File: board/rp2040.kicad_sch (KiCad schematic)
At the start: 22 parts, among them U1 W25Q128JVS, U2 RP2040, Y1 12MhZ

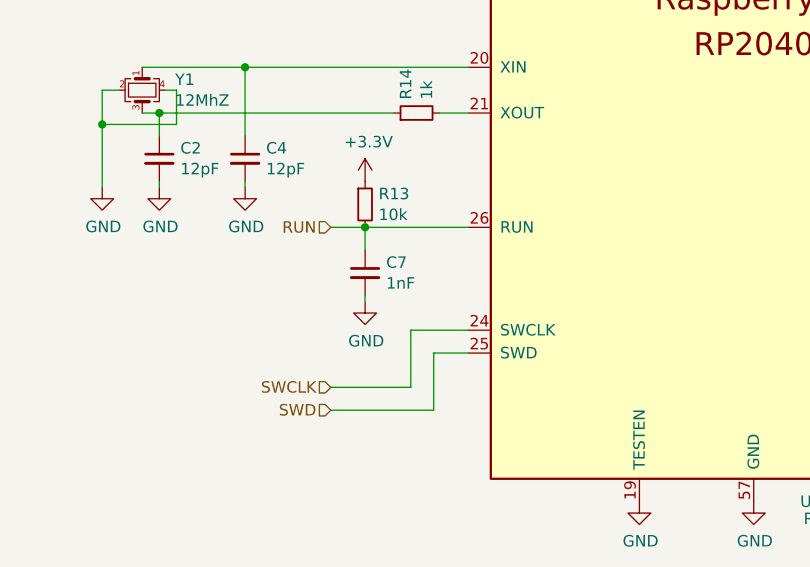
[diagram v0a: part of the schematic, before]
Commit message: added needle addapter
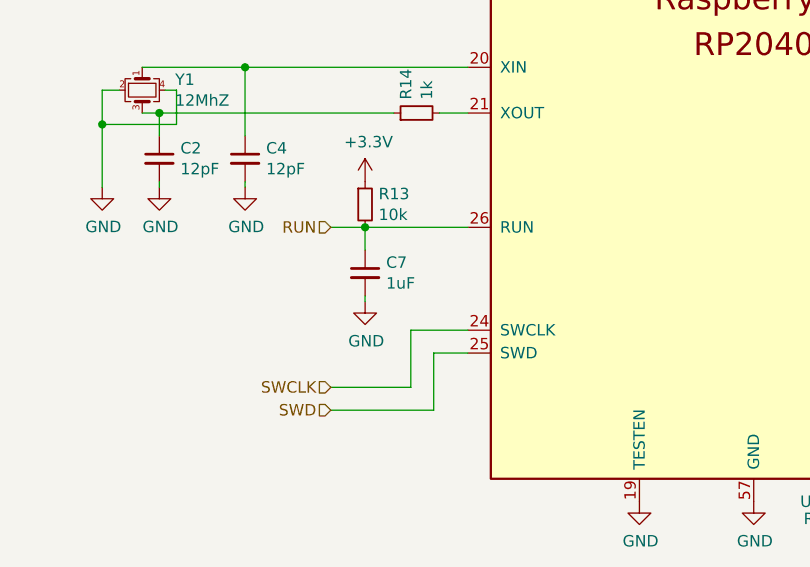
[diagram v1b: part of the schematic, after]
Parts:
- C7: value 1nF -> 1uF
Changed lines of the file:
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@@
       (effects (font (size 1.27 1.27)) (justify left))
     )
-    (property "Value" "1nF" (id 1) (at 92.5068 135.763 0)
+    (property "Value" "1uF" (id 1) (at 92.5068 135.763 0)
       (effects (font (size 1.27 1.27)) (justify left))
     )

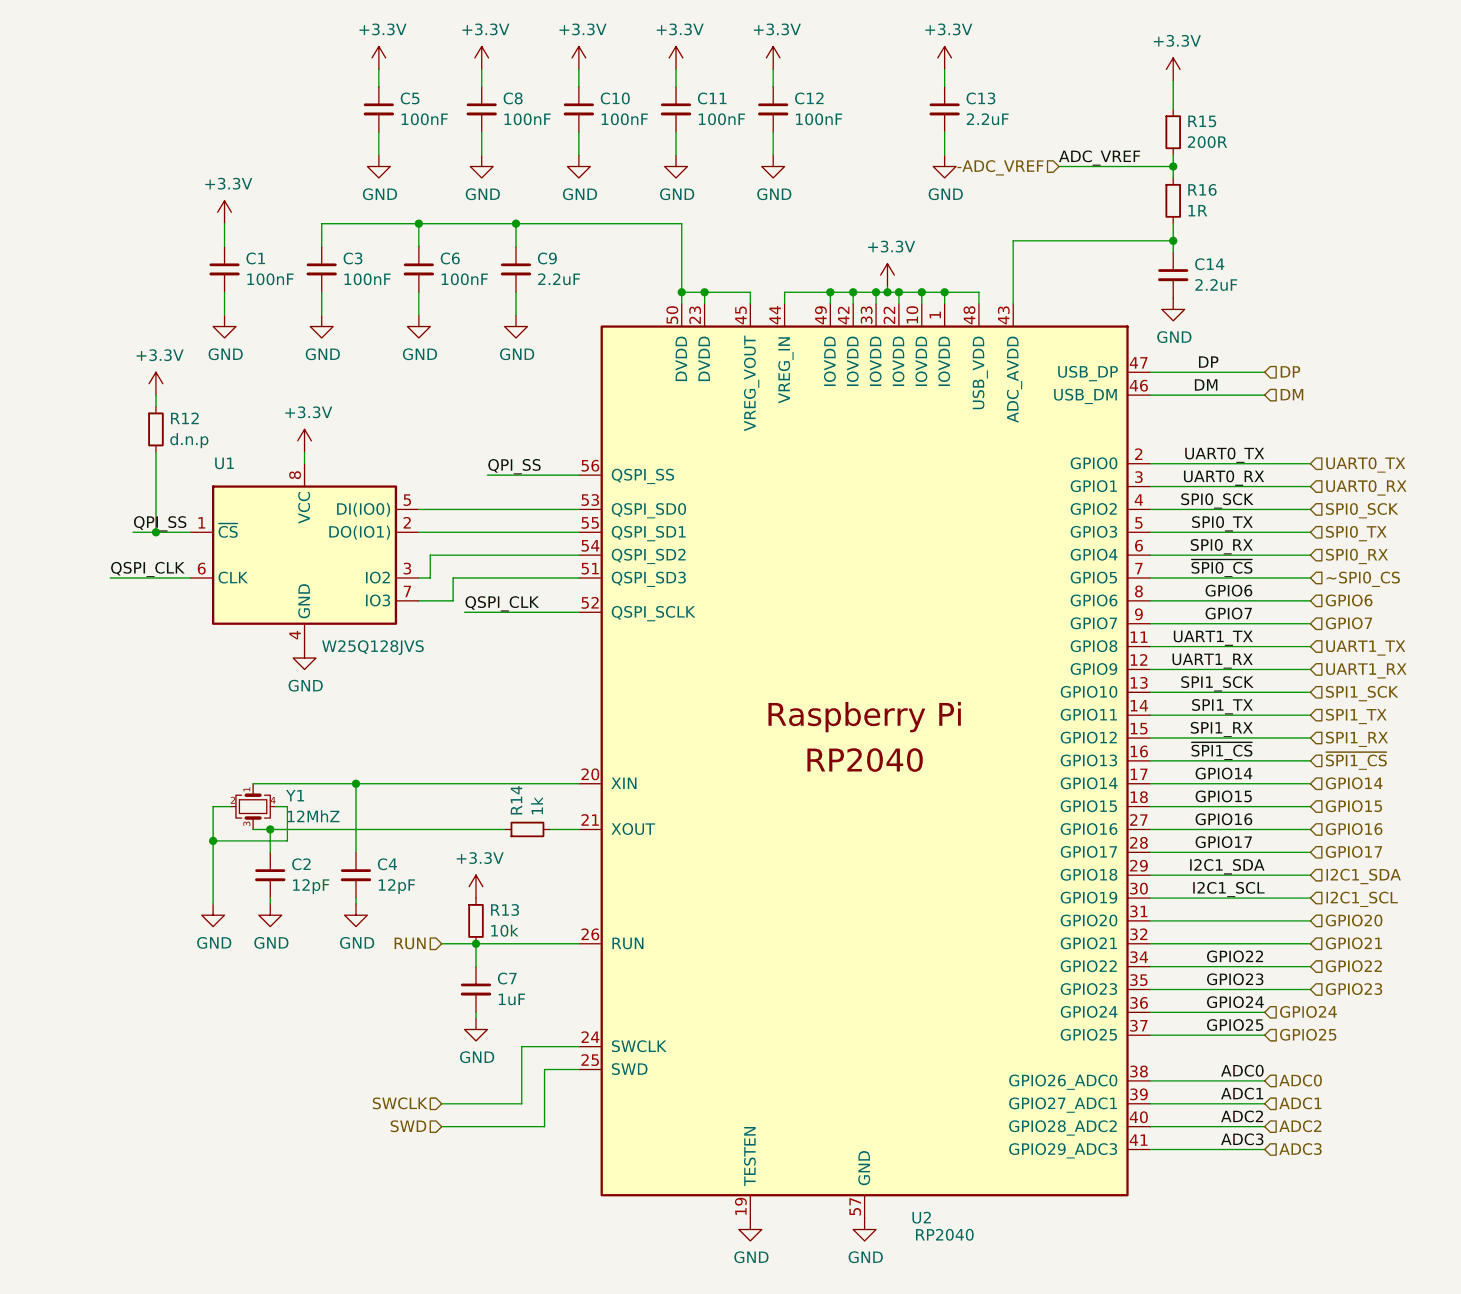
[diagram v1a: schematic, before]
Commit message: improved power integrity
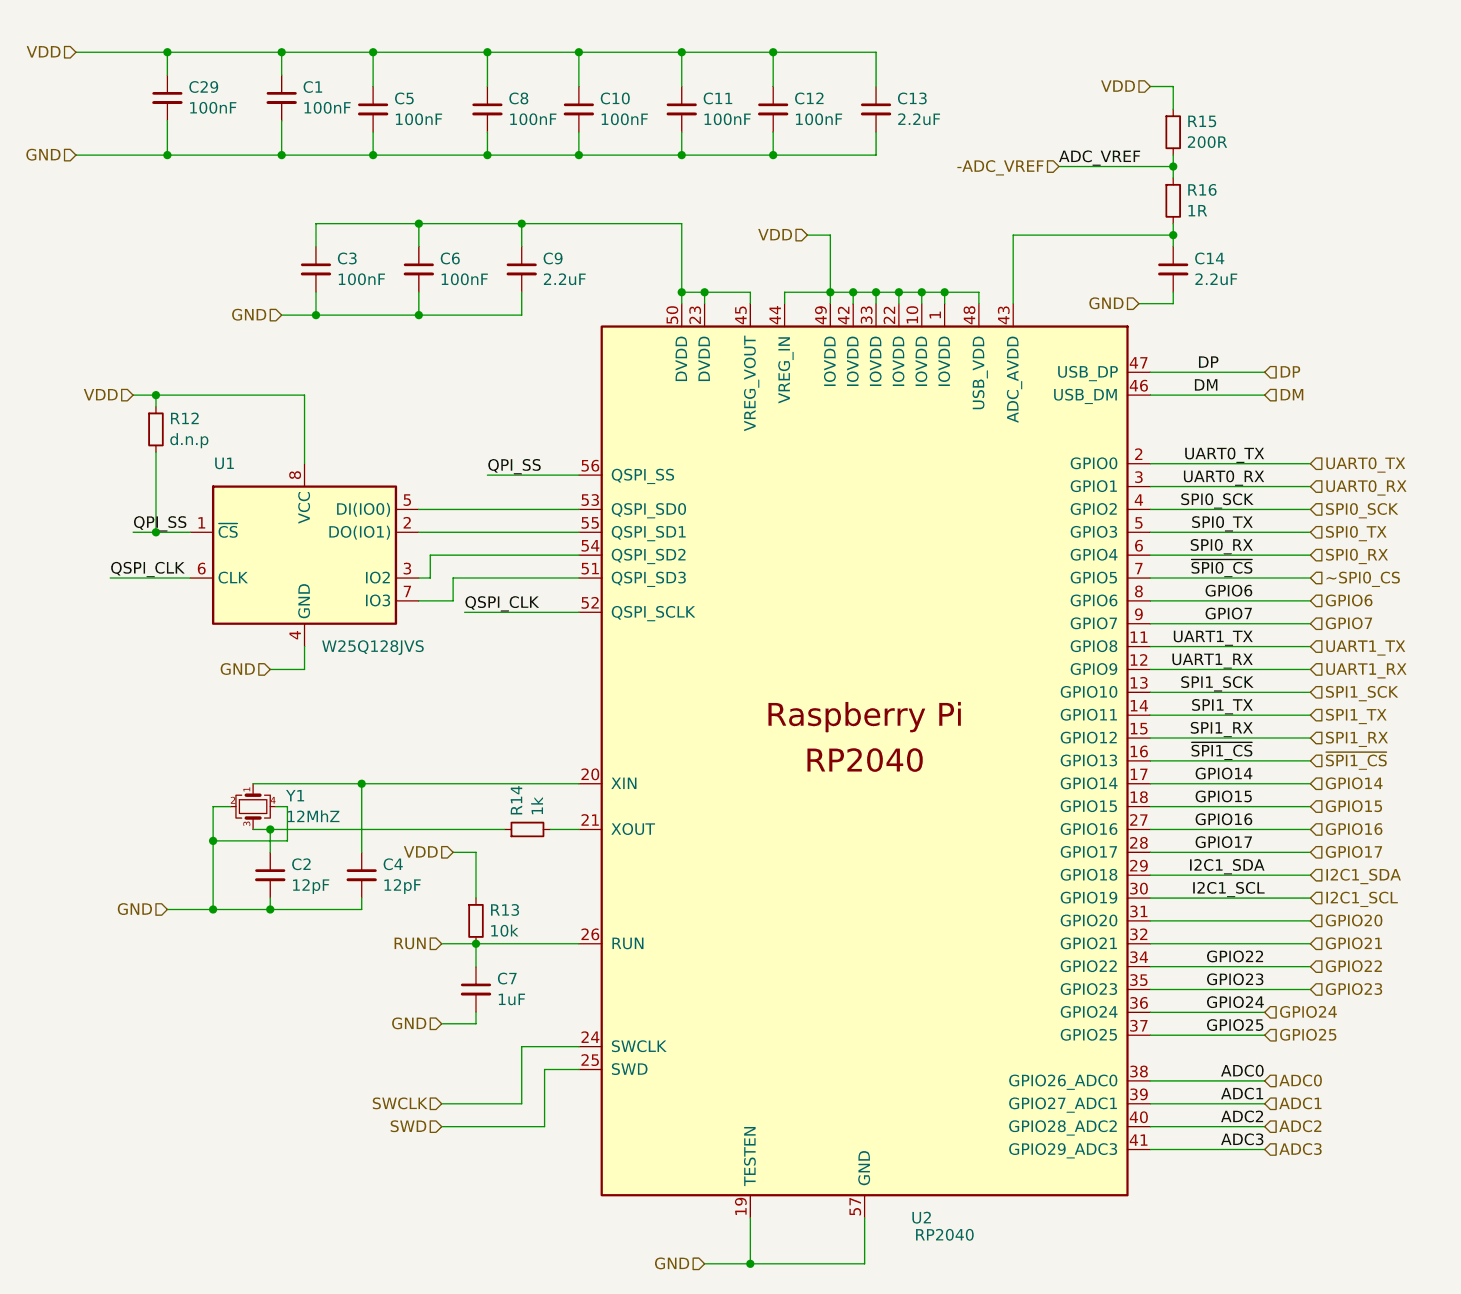
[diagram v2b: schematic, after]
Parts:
- added C29: 100nF, Capacitor_SMD:C_0603_1608Metric, symbol Device:C_Small
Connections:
- net GND: now also C29.2
- net +3V3 renamed VDD
- net VDD: now also C29.1
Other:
- moved on the sheet: C1, C11, C13, C14, C3, C4, C5, C8, C9

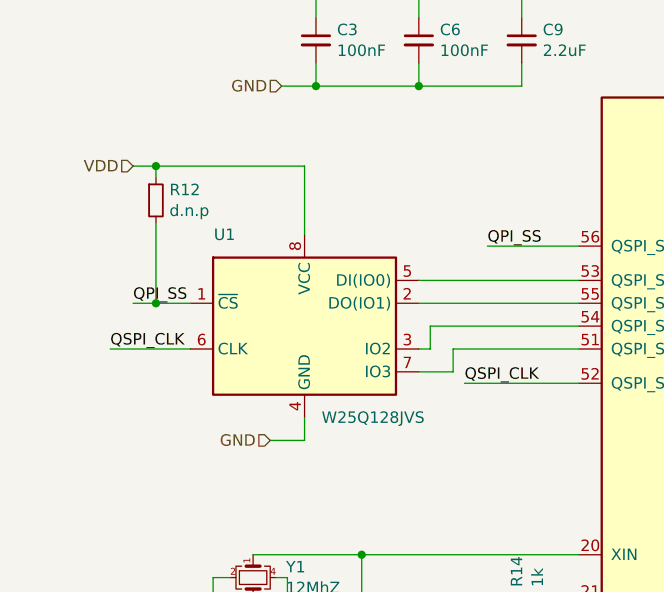
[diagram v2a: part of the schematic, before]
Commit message: added boot select button and standard (small) flash
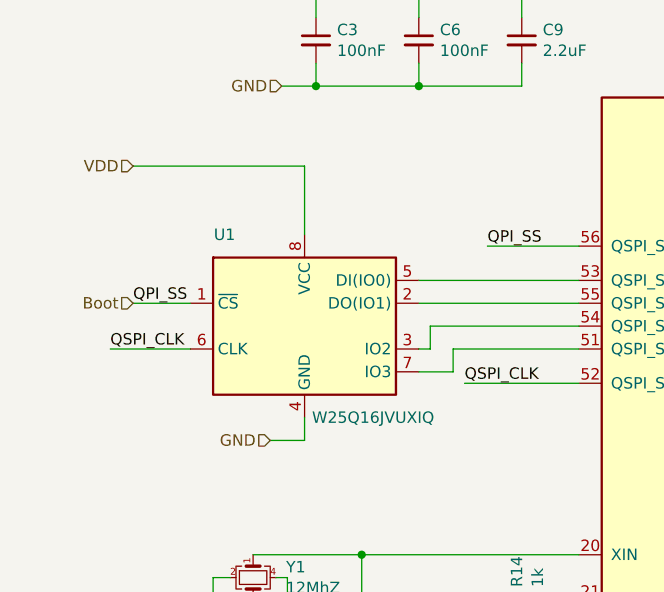
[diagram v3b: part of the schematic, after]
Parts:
- removed R12: d.n.p, Resistor_SMD:R_0603_1608Metric, symbol Device:R_Small
- U1: value W25Q128JVS -> W25Q16JVUXIQ; footprint Package_SO:SOIC-8_5.23x5.23mm_P1.27mm -> Package_DFN_QFN:DFN-8-1EP_3x2mm_P0.5mm_EP1.3x1.5mm
- U2: footprint b018:RP2040-QFN-56 -> Package_DFN_QFN:QFN-56-1EP_7x7mm_P0.4mm_EP3.2x3.2mm
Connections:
- net QPI_SS renamed Boot

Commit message: moved all components to top layer
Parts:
- C1, C10, C11, C12, C13, C14, C29, C3, C5, C6, C7, C8, C9: footprint Capacitor_SMD:C_0603_1608Metric -> Capacitor_SMD:C_0402_1005Metric
- R13, R14: footprint Resistor_SMD:R_0603_1608Metric -> Resistor_SMD:R_0402_1005Metric
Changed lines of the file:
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@@
       (effects (font (size 1.27 1.27)) (justify left))
     )
-    (property "Footprint" "Capacitor_SMD:C_0603_1608Metric" (at 55.88 35.56 0)
+    (property "Footprint" "Capacitor_SMD:C_0402_1005Metric" (at 55.88 35.56 0)
       (effects (font (size 1.27 1.27)) hide)
     )
@@
       (effects (font (size 1.27 1.27)) (justify left))
     )
-    (property "Footprint" "Capacitor_SMD:C_0603_1608Metric" (at 113.03 36.83 0)
+    (property "Footprint" "Capacitor_SMD:C_0402_1005Metric" (at 113.03 36.83 0)
       (effects (font (size 1.27 1.27)) hide)
     )
@@
       (effects (font (size 1.27 1.27)) (justify left))
     )
-    (property "Footprint" "Capacitor_SMD:C_0603_1608Metric" (at 134.62 36.83 0)
+    (property "Footprint" "Capacitor_SMD:C_0402_1005Metric" (at 134.62 36.83 0)
       (effects (font (size 1.27 1.27)) hide)
     )
@@
       (effects (font (size 1.27 1.27)) (justify left))
     )
-    (property "Footprint" "Capacitor_SMD:C_0603_1608Metric" (at 95.25 54.61 0)
+    (property "Footprint" "Capacitor_SMD:C_0402_1005Metric" (at 95.25 54.61 0)
       (effects (font (size 1.27 1.27)) hide)
     )
@@
       (effects (font (size 1.27 1.27)) (justify left))
     )
-    (property "Footprint" "Capacitor_SMD:C_0603_1608Metric" (at 101.6 36.83 0)
+    (property "Footprint" "Capacitor_SMD:C_0402_1005Metric" (at 101.6 36.83 0)
       (effects (font (size 1.27 1.27)) hide)
     )
@@
       (effects (font (size 1.27 1.27)) (justify left))
     )
-    (property "Footprint" "Capacitor_SMD:C_0603_1608Metric" (at 78.74 36.83 0)
+    (property "Footprint" "Capacitor_SMD:C_0402_1005Metric" (at 78.74 36.83 0)
       (effects (font (size 1.27 1.27)) hide)
     )
@@
       (effects (font (size 1.27 1.27)) (justify left))
     )
-    (property "Footprint" "Capacitor_SMD:C_0603_1608Metric" (at 90.17 134.62 0)
+    (property "Footprint" "Capacitor_SMD:C_0402_1005Metric" (at 90.17 134.62 0)
       (effects (font (size 1.27 1.27)) hide)
     )
@@
       (effects (font (size 1.27 1.27)) (justify left))
     )
-    (property "Footprint" "Capacitor_SMD:C_0603_1608Metric" (at 123.19 36.83 0)
+    (property "Footprint" "Capacitor_SMD:C_0402_1005Metric" (at 123.19 36.83 0)
       (effects (font (size 1.27 1.27)) hide)
     )
@@
       (effects (font (size 1.27 1.27)) (justify left))
     )
-    (property "Footprint" "Resistor_SMD:R_0603_1608Metric" (at 90.17 127 0)
+    (property "Footprint" "Resistor_SMD:R_0402_1005Metric" (at 90.17 127 0)
       (effects (font (size 1.27 1.27)) hide)
     )
@@
       (effects (font (size 1.27 1.27)) (justify left))
     )
-    (property "Footprint" "Capacitor_SMD:C_0603_1608Metric" (at 167.64 54.61 0)
+    (property "Footprint" "Capacitor_SMD:C_0402_1005Metric" (at 167.64 54.61 0)
       (effects (font (size 1.27 1.27)) hide)
     )
@@
       (effects (font (size 1.27 1.27)) (justify left))
     )
-    (property "Footprint" "Capacitor_SMD:C_0603_1608Metric" (at 68.58 35.56 0)
+    (property "Footprint" "Capacitor_SMD:C_0402_1005Metric" (at 68.58 35.56 0)
       (effects (font (size 1.27 1.27)) hide)
     )
@@
       (effects (font (size 1.27 1.27)) (justify left))
     )
-    (property "Footprint" "Capacitor_SMD:C_0603_1608Metric" (at 91.44 36.83 0)
+    (property "Footprint" "Capacitor_SMD:C_0402_1005Metric" (at 91.44 36.83 0)
       (effects (font (size 1.27 1.27)) hide)
     )
@@
       (effects (font (size 1.27 1.27)) (justify left))
     )
-    (property "Footprint" "Capacitor_SMD:C_0603_1608Metric" (at 83.82 54.61 0)
+    (property "Footprint" "Capacitor_SMD:C_0402_1005Metric" (at 83.82 54.61 0)
       (effects (font (size 1.27 1.27)) hide)
     )
@@
       (effects (font (size 1.27 1.27)) (justify left))
     )
-    (property "Footprint" "Resistor_SMD:R_0603_1608Metric" (at 95.885 116.84 0)
+    (property "Footprint" "Resistor_SMD:R_0402_1005Metric" (at 95.885 116.84 0)
       (effects (font (size 1.27 1.27)) hide)
     )
@@
       (effects (font (size 1.27 1.27)) (justify left))
     )
-    (property "Footprint" "Capacitor_SMD:C_0603_1608Metric" (at 72.39 54.61 0)
-      (effects (font (size 1.27 1.27)) hide)
-    )
+    (property "Footprint" "Capacitor_SMD:C_0402_1005Metric" (at 72.39 54.61 0)
+      (effects (font (size 1.27 1.27)) hide)
+    )

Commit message: added lcsc part numbers
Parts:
- C1, C10, C11, C12, C29, C3, C5, C6, C8: lcsc (none) -> C1525
- C13, C14, C9: lcsc (none) -> C12530
- C2, C4: lcsc (none) -> C1644
- C7: lcsc (none) -> C52923
- R13: lcsc (none) -> C25744
- R14: lcsc (none) -> C11702
- R15: lcsc (none) -> C8218
- R16: lcsc (none) -> C22936
- U1: lcsc (none) -> C2843335
- U2: lcsc (none) -> C2040
- Y1: lcsc (none) -> C9002
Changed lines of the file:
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@@
+      (effects (font (size 1.27 1.27)) hide)
+    )
+    (property "lcsc" "C1525" (at 55.88 35.56 0)
       (effects (font (size 1.27 1.27)) hide)
     )
@@
       (effects (font (size 1.27 1.27)) hide)
     )
+    (property "lcsc" "C1525" (at 113.03 36.83 0)
+      (effects (font (size 1.27 1.27)) hide)
+    )
     (pin "1")
     (pin "2")
@@
       (effects (font (size 1.27 1.27)) hide)
     )
+    (property "lcsc" "C12530" (at 134.62 36.83 0)
+      (effects (font (size 1.27 1.27)) hide)
+    )
     (pin "1")
     (pin "2")
@@
       (effects (font (size 1.27 1.27)) hide)
     )
+    (property "lcsc" "C8218" (at 167.64 39.37 0)
+      (effects (font (size 1.27 1.27)) hide)
+    )
     (pin "1")
     (pin "2")
@@
       (effects (font (size 1.27 1.27)) hide)
     )
+    (property "lcsc" "C12530" (at 95.25 54.61 0)
+      (effects (font (size 1.27 1.27)) hide)
+    )
     (pin "1")
     (pin "2")
@@
     )
     (property "Datasheet" "~" (at 101.6 36.83 0)
+      (effects (font (size 1.27 1.27)) hide)
+    )
+    (property "lcsc" "C1525" (at 101.6 36.83 0)
       (effects (font (size 1.27 1.27)) hide)
     )
@@
     )
     (property "Datasheet" "" (at 114.3 109.22 0)
+      (effects (font (size 1.27 1.27)) hide)
+    )
+    (property "lcsc" "C2040" (at 133.35 109.22 0)
       (effects (font (size 1.27 1.27)) hide)
     )
@@
       (effects (font (size 1.27 1.27)) hide)
     )
+    (property "lcsc" "C1525" (at 78.74 36.83 0)
+      (effects (font (size 1.27 1.27)) hide)
+    )
     (pin "1")
     (pin "2")
@@
       (effects (font (size 1.27 1.27)) hide)
     )
+    (property "lcsc" "C52923" (at 90.17 134.62 0)
+      (effects (font (size 1.27 1.27)) hide)
+    )
     (pin "1")
     (pin "2")
@@
     )
     (property "Datasheet" "~" (at 77.47 121.92 0)
+      (effects (font (size 1.27 1.27)) hide)
+    )
+    (property "lcsc" "C1644" (at 77.47 121.92 0)
       (effects (font (size 1.27 1.27)) hide)
     )
@@
     )
     (property "Datasheet" "https://www.winbond.com/resource-files/w25q16jv%20spi%20revh%2004082019%20plus.pdf" (at 71.12 86.36 0)
+      (effects (font (size 1.27 1.27)) hide)
+    )
+    (property "lcsc" "C2843335" (at 71.12 86.36 0)
       (effects (font (size 1.27 1.27)) hide)
     )
@@
       (effects (font (size 1.27 1.27)) hide)
     )
+    (property "lcsc" "C1525" (at 123.19 36.83 0)
+      (effects (font (size 1.27 1.27)) hide)
+    )
     (pin "1")
     (pin "2")
@@
     )
     (property "MPN" "ABM8G-12.000MHZ-4Y-T3" (at 65.405 114.3 90)
+      (effects (font (size 1.27 1.27)) hide)
+    )
+    (property "lcsc" "C9002" (at 65.405 114.3 0)
       (effects (font (size 1.27 1.27)) hide)
     )
@@
       (effects (font (size 1.27 1.27)) hide)
     )
+    (property "lcsc" "C25744" (at 90.17 127 0)
+      (effects (font (size 1.27 1.27)) hide)
+    )
     (pin "1")
     (pin "2")
@@
       (effects (font (size 1.27 1.27)) hide)
     )
+    (property "lcsc" "C12530" (at 167.64 54.61 0)
+      (effects (font (size 1.27 1.27)) hide)
+    )
     (pin "1")
     (pin "2")
@@
       (effects (font (size 1.27 1.27)) hide)
     )
+    (property "lcsc" "C1525" (at 68.58 35.56 0)
+      (effects (font (size 1.27 1.27)) hide)
+    )
     (pin "1")
     (pin "2")
@@
       (effects (font (size 1.27 1.27)) hide)
     )
+    (property "lcsc" "C1644" (at 67.31 121.92 0)
+      (effects (font (size 1.27 1.27)) hide)
+    )
     (pin "1")
     (pin "2")
@@
       (effects (font (size 1.27 1.27)) hide)
     )
+    (property "lcsc" "C1525" (at 91.44 36.83 0)
+      (effects (font (size 1.27 1.27)) hide)
+    )
     (pin "1")
     (pin "2")
@@
       (effects (font (size 1.27 1.27)) hide)
     )
+    (property "lcsc" "C1525" (at 83.82 54.61 0)
+      (effects (font (size 1.27 1.27)) hide)
+    )
     (pin "1")
     (pin "2")
@@
       (effects (font (size 1.27 1.27)) hide)
     )
+    (property "lcsc" "C22936" (at 167.64 46.99 0)
+      (effects (font (size 1.27 1.27)) hide)
+    )
     (pin "1")
     (pin "2")
@@
       (effects (font (size 1.27 1.27)) hide)
     )
+    (property "lcsc" "C11702" (at 95.885 116.84 0)
+      (effects (font (size 1.27 1.27)) hide)
+    )
     (pin "1")
     (pin "2")
@@
       (effects (font (size 1.27 1.27)) hide)
     )
+    (property "lcsc" "C1525" (at 72.39 54.61 0)
+      (effects (font (size 1.27 1.27)) hide)
+    )
